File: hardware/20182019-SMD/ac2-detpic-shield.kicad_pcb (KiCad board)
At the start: 2 copper layers, 99.1 x 69.6 mm, 79 parts, among them J1 HEADER, J2 HEADER, J3 HEADER, J4 HEADER, J5 HEADER, J6 HEADER, J7 HEADER, J8 MPLAB ICD3, M1 M1, M2 M2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

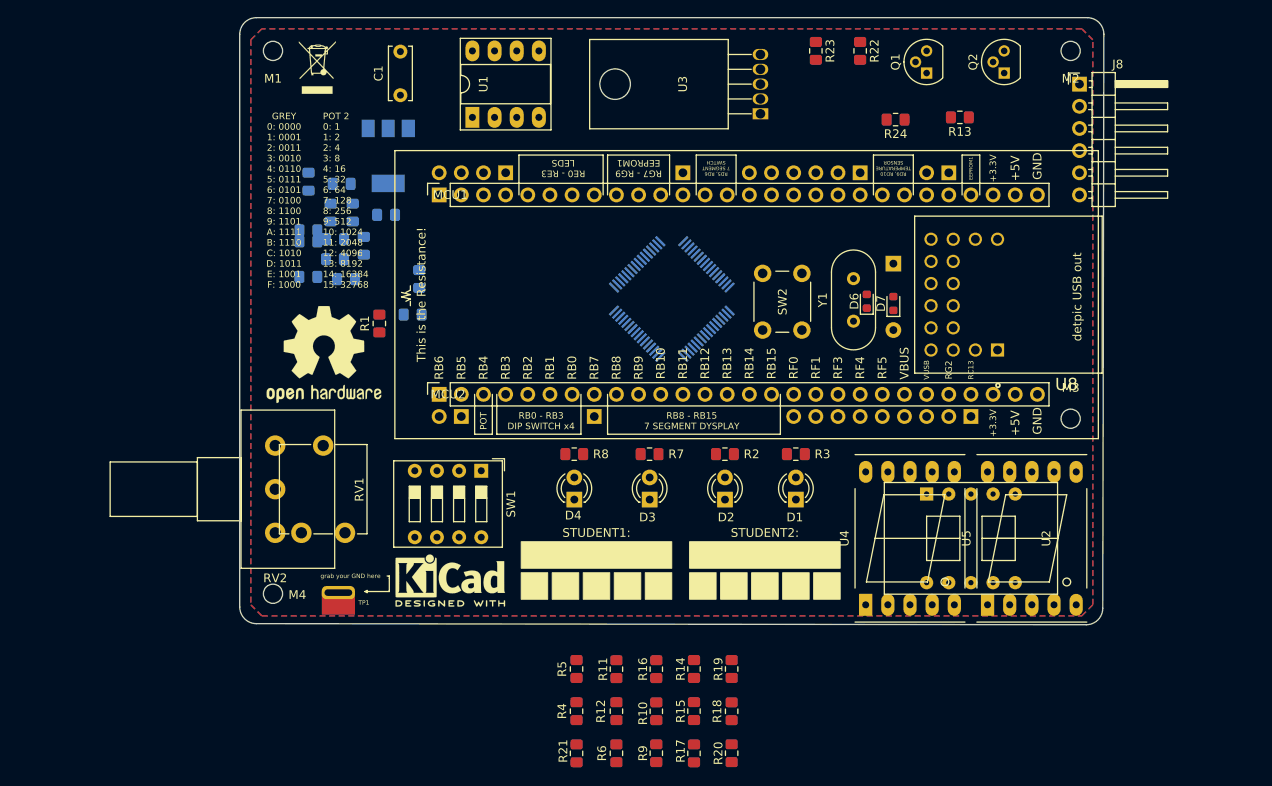
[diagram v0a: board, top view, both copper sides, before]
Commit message: added some routing
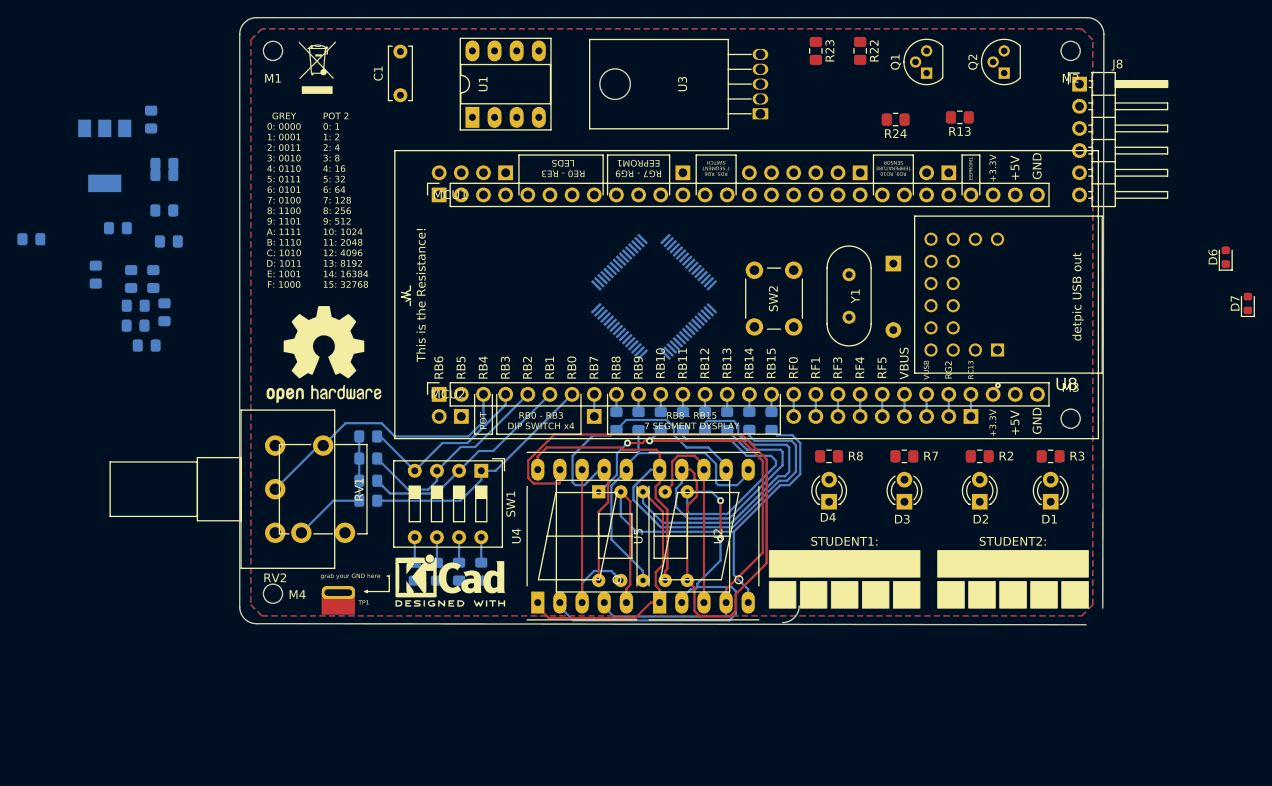
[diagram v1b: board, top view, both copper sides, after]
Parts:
- R1, R10, R11, R12, R14, R15, R16, R17, R18, R19, R20, R21, R4, R5, R6, R9: moved to B.Cu
- moved R27 44.6 mm to (103.1, 50.8)
- moved R21 44.2 mm to (188.0, 71.6), turned to 90 degrees
- moved D6 41.5 mm to (240.0, 52.9)
- moved D7 40.6 mm to (242.6, 58.2)
- moved R6 40.6 mm to (141.7, 80.8), turned to 180 degrees
- moved R20 38.2 mm to (185.4, 71.6), turned to 90 degrees
- moved R17 38.1 mm to (177.8, 71.6), turned to 90 degrees
- moved U2 37.6 mm to (173.2, 84.8)
- moved U4 37.6 mm to (161.2, 92.5)
- moved U5 37.6 mm to (175.1, 92.5)
- moved R4 37.5 mm to (141.7, 75.9), turned to 180 degrees
- moved C7 35.8 mm to (116.8, 37.1)
- moved R15 33.9 mm to (172.7, 71.6), turned to 90 degrees
- moved R18 33.4 mm to (180.3, 71.6)
- moved U7 32.5 mm to (111.5, 41.2)
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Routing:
- net /7F: track 0.00 -> 109.3 mm
- net /7D: track 0.00 -> 74.8 mm, vias 0 -> 2
- net /7G: track 0.00 -> 69.5 mm
- net /7E: track 0.00 -> 67.0 mm
- net /7C: track 0.00 -> 59.8 mm, vias 0 -> 2
- net /7DP: track 0.00 -> 56.5 mm
- net /7A: track 0.00 -> 44.9 mm
- net /7B: track 0.00 -> 36.5 mm
- net /RB4: track 0.00 -> 31.5 mm
- net /RB0: track 0.00 -> 28.0 mm
- net /RB1: track 0.00 -> 25.1 mm
- net /RB2: track 0.00 -> 23.9 mm
- net /7C2: track 0.00 -> 23.9 mm
- net /7C1: track 0.00 -> 23.0 mm
- net /RB3: track 0.00 -> 20.7 mm
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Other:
- outline, holes or cut-outs redrawn
- board text added: "In case this board is lost, deliver it to someone at the Electronics, Telecomunications and Informatics department’s secretary"
- board text removed: "In case this board is lost, deliver it to someone at the Electronics, Telecomunications and Informatics department's secretary"

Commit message: pcb work
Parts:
- U6: moved to F.Cu
- moved R27 134.8 mm to (237.7, 57.9)
- moved R26 127.0 mm to (239.3, 63.2), turned to 0 degrees
- moved U7 79.5 mm to (190.2, 52.6), turned to 90 degrees
- moved C11 79.2 mm to (196.9, 64.8), turned to 180 degrees
- moved C10 78.8 mm to (196.9, 49.8)
- moved C2 77.4 mm to (191.5, 63.5), turned to 0 degrees
- moved C8 76.5 mm to (191.5, 58.9), turned to 0 degrees
- moved C7 74.6 mm to (187.4, 61.2), turned to 180 degrees
- moved C3 74.5 mm to (184.9, 52.6), turned to 270 degrees
- moved C5 74.4 mm to (191.5, 61.2), turned to 0 degrees
- moved C6 72.1 mm to (187.0, 65.0), turned to 225 degrees
- moved C4 70.4 mm to (187.4, 58.9), turned to 180 degrees
- moved R25 51.7 mm to (166.4, 50.0), turned to 45 degrees
- moved C12 46.8 mm to (159.3, 65.0), turned to 180 degrees
- moved C9 44.8 mm to (163.1, 62.0), turned to 0 degrees
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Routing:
- net /+5V_EXT: track 0.00 -> 60.3 mm
- net /RG3: track 0.00 -> 42.5 mm
- net /RF1: track 2.54 -> 40.1 mm
- net /RG2: track 2.54 -> 37.8 mm
- net /RD8: track 0.00 -> 35.0 mm
- net GND: track 15.5 -> 50.5 mm
- net /VUSB: track 2.54 -> 35.6 mm
- net /RF0: track 2.54 -> 35.5 mm
- net /RD9: track 0.00 -> 31.8 mm
- net /VBUS: track 2.54 -> 34.0 mm
- net /RC15: track 0.00 -> 28.7 mm
- net /RD10: track 0.00 -> 28.4 mm
- net /RC12: track 0.00 -> 27.2 mm
- net /RD11: track 0.00 -> 25.3 mm
- net /RF3: track 2.54 -> 27.1 mm
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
